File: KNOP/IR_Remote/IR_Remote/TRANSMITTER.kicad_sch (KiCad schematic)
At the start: 18 parts, among them Q1 BC337, SW1 SW_Push, T1 BC327

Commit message: knops schematic chnages
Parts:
- removed BT1: 9V_Batt, symbol Device:Battery
- added J1, J2: Conn_01x01_Pin, symbol Connector:Conn_01x01_Pin
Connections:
- net THR is gone; now on net GND: C3.2
- net GND: now also J2.1 (Pin_1); no longer C2.2, IO1.2 (TR), IO1.6 (THR), R4.2
- net at R1.1: now also J1.1 (Pin_1)
- new net TR: C2.2, IO1.2 (TR), IO1.6 (THR), R4.2
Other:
- note added: "9V"
- note added: "GND"
- note added: "VCC"

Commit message: idk
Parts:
- C1: footprint Capacitor_Tantalum_SMD:CP_EIA-3216-18_Kemet-A_Pad1.58x1.35mm_HandSolder -> Capacitor_THT:CP_Radial_D6.3mm_P2.50mm
- SW1: footprint (none) -> Button_Switch_THT:SW_PUSH_6mm_H5mm
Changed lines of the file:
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@@
 			)
 		)
-		(property "Footprint" ""
+		(property "Footprint" "Button_Switch_THT:SW_PUSH_6mm_H5mm"
 			(at 59.69 85.09 0)
 			(effects
@@
 		)
 		(instances
-			(project ""
+			(project "IR_Remote"
 				(path "/07d62ec6-6e59-42d0-a028-2e4cdf5deb8a/a4503051-c576-4a05-ab54-d863fe682058"
 					(reference "SW1")
@@
 		)
 		(instances
-			(project ""
+			(project "IR_Remote"
 				(path "/07d62ec6-6e59-42d0-a028-2e4cdf5deb8a/a4503051-c576-4a05-ab54-d863fe682058"
 					(reference "#PWR012")
@@
 		)
 		(instances
-			(project ""
+			(project "IR_Remote"
 				(path "/07d62ec6-6e59-42d0-a028-2e4cdf5deb8a/a4503051-c576-4a05-ab54-d863fe682058"
 					(reference "J1")
@@
 		)
 		(instances
-			(project ""
+			(project "IR_Remote"
 				(path "/07d62ec6-6e59-42d0-a028-2e4cdf5deb8a/a4503051-c576-4a05-ab54-d863fe682058"
 					(reference "IO1")
@@
 		)
 		(instances
-			(project ""
+			(project "IR_Remote"
 				(path "/07d62ec6-6e59-42d0-a028-2e4cdf5deb8a/a4503051-c576-4a05-ab54-d863fe682058"
 					(reference "T1")
@@
 			)
 		)
-		(property "Footprint" "Capacitor_Tantalum_SMD:CP_EIA-3216-18_Kemet-A_Pad1.58x1.35mm_HandSolder"
+		(property "Footprint" "Capacitor_THT:CP_Radial_D6.3mm_P2.50mm"
 			(at 52.3748 100.33 0)
 			(effects
@@
 		)
 		(instances
-			(project ""
+			(project "IR_Remote"
 				(path "/07d62ec6-6e59-42d0-a028-2e4cdf5deb8a/a4503051-c576-4a05-ab54-d863fe682058"
 					(reference "Q1")
@@
 		)
 		(instances
-			(project ""
+			(project "IR_Remote"
 				(path "/07d62ec6-6e59-42d0-a028-2e4cdf5deb8a/a4503051-c576-4a05-ab54-d863fe682058"
 					(reference "D2")

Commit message: idk
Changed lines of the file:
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@@
 		(dnp no)
 		(property "Reference" "C3"
-			(at 105.41 99.06 0)
+			(at 105.41 99.695 0)
 			(effects
 				(font
@@
 		(dnp no)
 		(property "Reference" "C1"
-			(at 60.325 95.25 0)
+			(at 59.055 95.25 0)
 			(effects
 				(font
@@
 		)
 		(property "Value" "VCC"
-			(at 107.315 106.045 0)
+			(at 110.49 107.95 0)
 			(effects
 				(font
@@
 		(dnp no)
 		(property "Reference" "R2"
-			(at 148.59 86.995 90)
+			(at 148.59 87.63 90)
 			(effects
 				(font
@@
 		)
 		(property "Value" "47R"
-			(at 149.225 88.9 90)
+			(at 149.225 89.535 90)
 			(effects
 				(font
@@
 		(dnp no)
 		(property "Reference" "C2"
-			(at 97.79 96.52 0)
+			(at 97.79 93.98 0)
 			(effects
 				(font
@@
 		)
 		(property "Value" "100p"
-			(at 97.79 93.98 0)
-			(effects
-				(font
+			(at 97.79 95.885 0)
+			(effects
+				(font

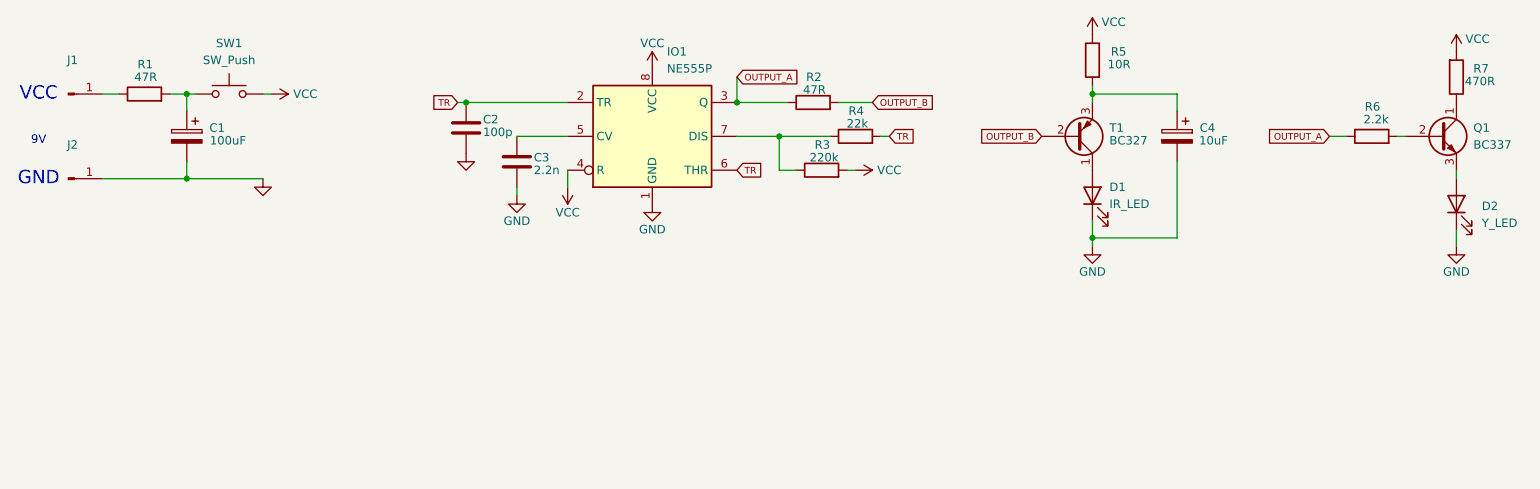
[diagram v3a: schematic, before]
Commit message: IR Remote updates
IR RX and TX PCB updates
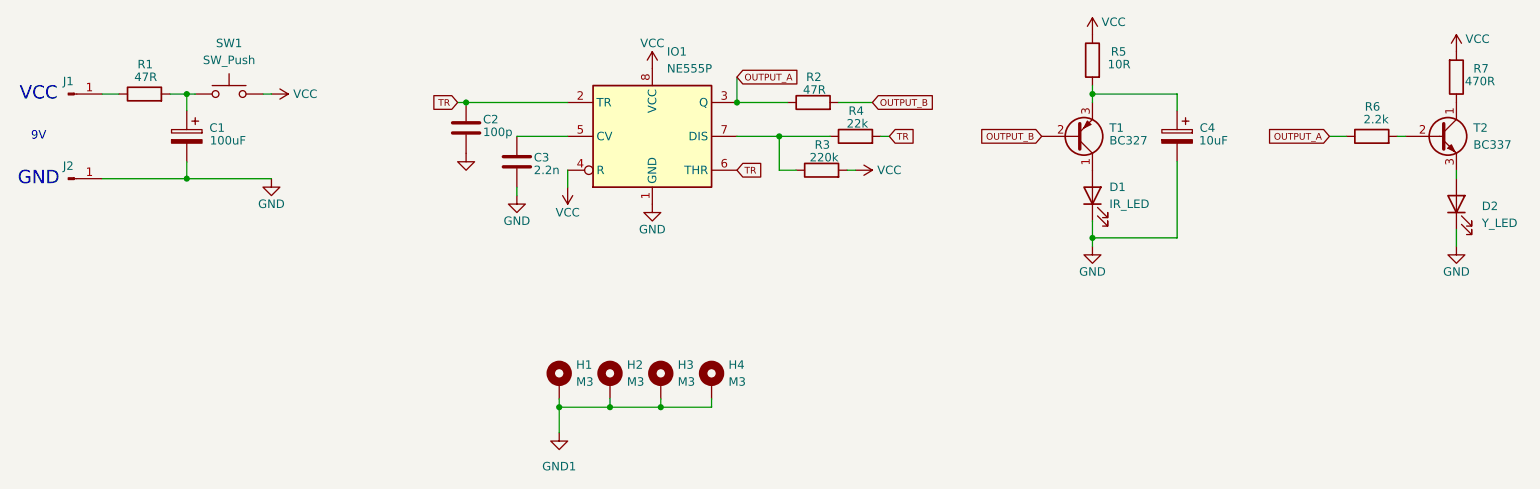
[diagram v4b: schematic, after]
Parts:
- added H1, H2, H3, H4: M3, MountingHole:MountingHole_3.2mm_M3_ISO7380_Pad, symbol Mechanical:MountingHole_Pad
- C2: footprint (none) -> Capacitor_THT:C_Disc_D4.3mm_W1.9mm_P5.00mm
- C3: footprint (none) -> Capacitor_THT:C_Disc_D5.0mm_W2.5mm_P5.00mm
- C4: footprint Capacitor_Tantalum_SMD:CP_EIA-3216-18_Kemet-A_Pad1.58x1.35mm_HandSolder -> Capacitor_THT:CP_Radial_D6.3mm_P2.50mm
- D1: footprint (none) -> LED_THT:LED_D5.0mm_Horizontal_O1.27mm_Z3.0mm_Clear
- D2: footprint (none) -> LED_THT:LED_D5.0mm
- J1, J2: footprint (none) -> Connector_Wire:SolderWire-0.5sqmm_1x01_D0.9mm_OD2.3mm
- R1, R2, R3, R4, R5, R6, R7: footprint Resistor_SMD:R_0805_2012Metric_Pad1.20x1.40mm_HandSolder -> Resistor_THT:R_Axial_DIN0207_L6.3mm_D2.5mm_P10.16mm_Horizontal
- T1: footprint Package_TO_SOT_THT:TO-92_Inline -> Package_TO_SOT_THT:TO-92_Inline_Wide
- T2: renamed from Q1; footprint Package_TO_SOT_THT:TO-92_Inline -> Package_TO_SOT_THT:TO-92_Inline_Wide
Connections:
- new net GND1: H1.1, H2.1, H3.1, H4.1
